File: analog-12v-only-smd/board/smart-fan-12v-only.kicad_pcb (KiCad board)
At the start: 2 copper layers, 62.2 x 41.3 mm, 31 parts, among them J1 KTY81/120, J2 12V_PWR, J3 12V_In, J4 FAN_Out, J5 FAN_Out, Q1 2N7000, Q2 FQP27P06, U1 LM358, U2 L7809, U3 NE555P

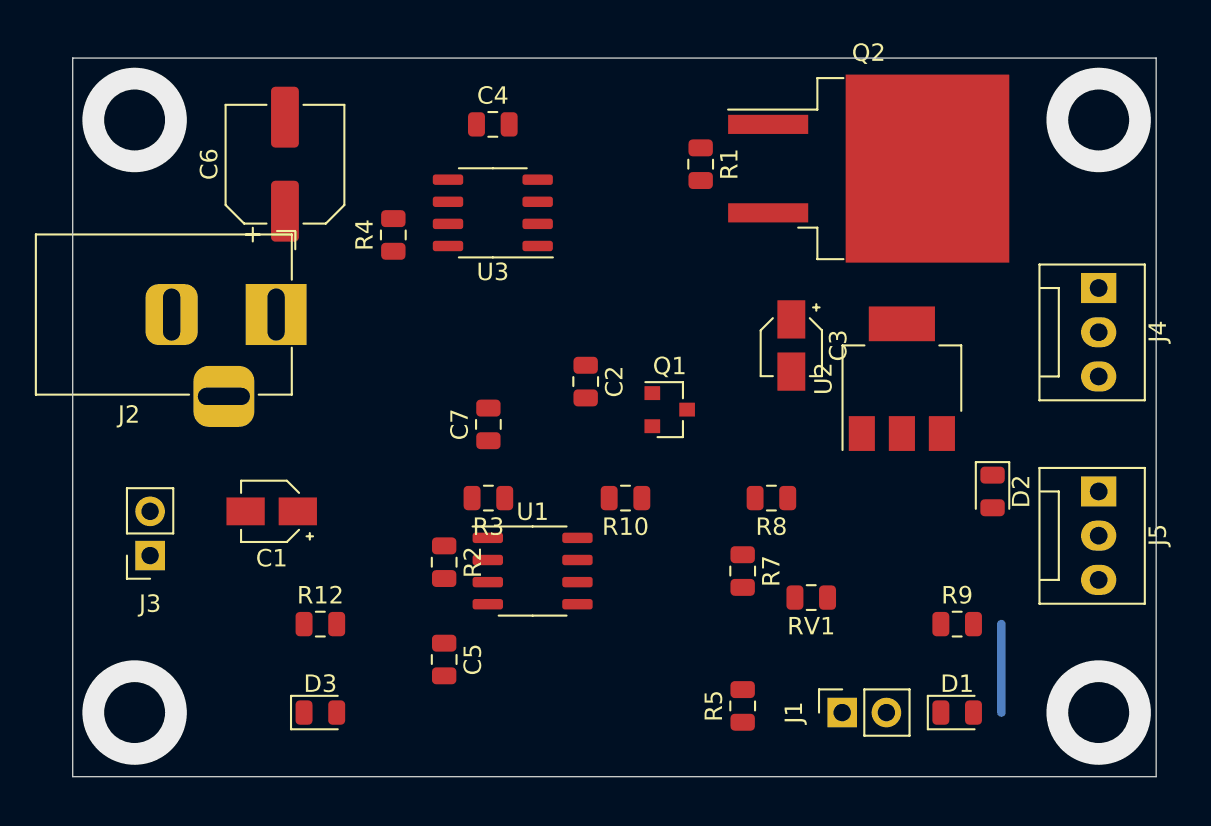
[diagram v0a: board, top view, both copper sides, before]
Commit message: Fix board layout
Power transistor drain-source swapped
Flyback diode reversed
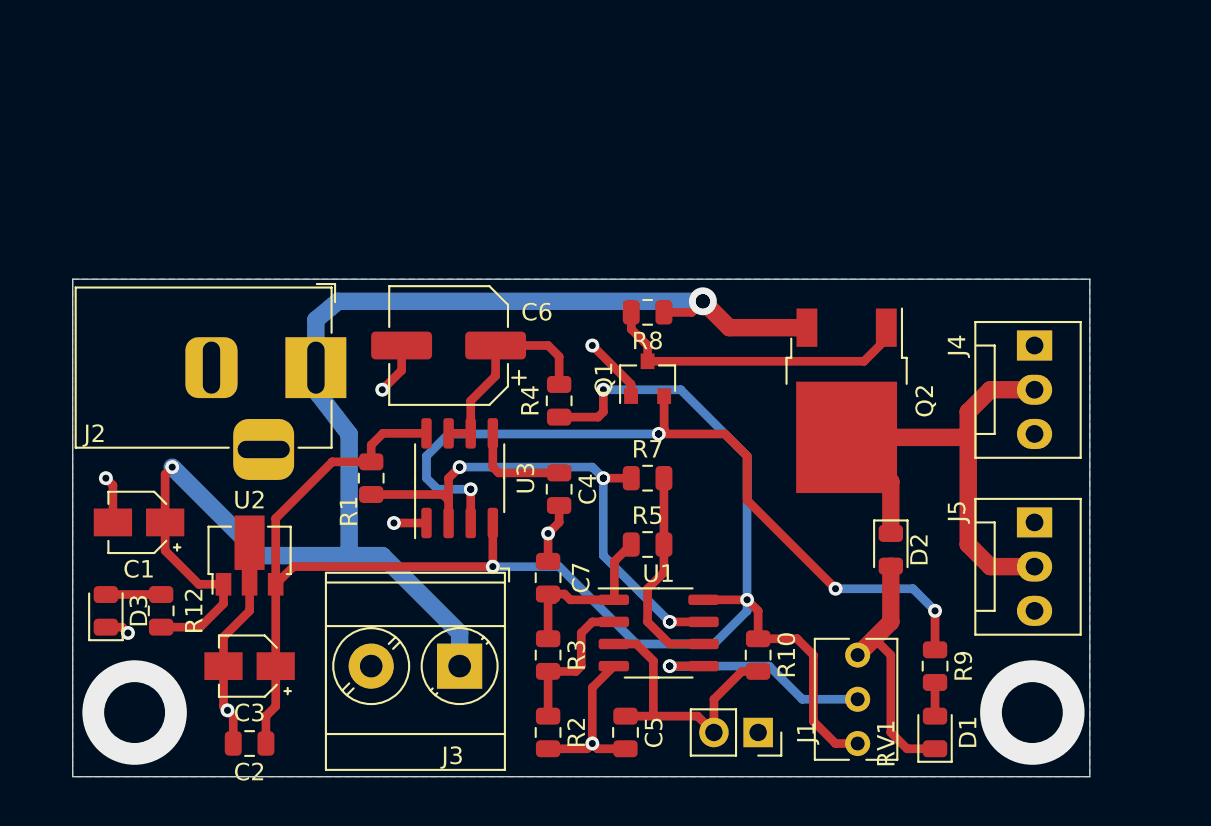
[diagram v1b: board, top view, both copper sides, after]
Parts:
- J3: footprint Connector_PinSocket_2.54mm:PinSocket_1x02_P2.54mm_Vertical -> TerminalBlock_Phoenix:TerminalBlock_Phoenix_MKDS-3-2-5.08_1x02_P5.08mm_Horizontal
- Q2: value FQP27P06 -> SUD19P06-60; footprint Package_TO_SOT_SMD:TO-263-2 -> Package_TO_SOT_SMD:TO-252-2
- R12: value 27k -> 5k
- R9: value 27k -> 3k3
- RV1: footprint Resistor_SMD:R_0805_2012Metric -> Potentiometer_THT:Potentiometer_Bourns_3266Y_Vertical
- U2: footprint Package_TO_SOT_SMD:SOT-223 -> Package_TO_SOT_SMD:SOT-89-3
- moved U2 38.8 mm to (114.8, 106.6)
- moved C3 36.2 mm to (114.8, 112.9), turned to 180 degrees
- moved C2 28.4 mm to (114.8, 117.3), turned to 180 degrees
- moved R1 26.1 mm to (121.8, 102.1)
- moved C4 21.3 mm to (132.6, 102.7), turned to 270 degrees
- moved J3 18.9 mm to (126.9, 112.9)
- moved U3 15.4 mm to (126.9, 102.1), turned to 90 degrees
- moved C6 14.0 mm to (126.2, 94.5), turned to 180 degrees
- moved D3 13.6 mm to (106.6, 109.7), turned to 90 degrees
- moved R4 13.5 mm to (132.6, 97.7)
- moved Q2 13.4 mm to (149.1, 97.7), turned to 270 degrees
- moved R8 12.8 mm to (137.7, 92.6)
- moved R10 11.8 mm to (144.0, 112.3), turned to 270 degrees
- moved R2 11.5 mm to (132.0, 116.7)
- moved C5 11.2 mm to (136.4, 116.7)
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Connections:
- D2 pad 1: GND -> Net-(D2-Pad1)
- D2 pad 2: Net-(D2-Pad2) -> GND
- J4 pad 2: Net-(D2-Pad2) -> Net-(D2-Pad1)
- J5 pad 2: Net-(D2-Pad2) -> Net-(D2-Pad1)
- Q2 pad 2: +12V -> Net-(D2-Pad1)
- Q2 pad 3: Net-(D2-Pad2) -> +12V
- R9 pad 1: Net-(D2-Pad2) -> Net-(Q1-Pad2)
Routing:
- net +9V: track 0.00 -> 95.1 mm, vias 0 -> 3
- net +12V: track 0.00 -> 82.6 mm, vias 0 -> 3
- net GND: track 0.00 -> 50.6 mm, vias 0 -> 8
- net Net-(Q1-Pad2): track 0.00 -> 46.0 mm, vias 0 -> 7
- net Trigger: track 0.00 -> 29.9 mm, vias 0 -> 8
- net Net-(D2-Pad1): track 0.00 -> 29.9 mm
- net Net-(Q1-Pad3): track 0.00 -> 18.1 mm
- net /TMP_IN: track 0.00 -> 16.4 mm
- net Net-(RV1-Pad2): track 0.00 -> 13.5 mm, vias 0 -> 3
- net Net-(C6-Pad1): track 0.00 -> 12.4 mm
- net Net-(R5-Pad2): track 0.00 -> 12.4 mm
- net Net-(C7-Pad1): track 0.00 -> 10.5 mm
- net Net-(R2-Pad1): track 0.00 -> 8.64 mm
- net Net-(C4-Pad1): track 0.00 -> 5.89 mm
- net Net-(D3-Pad2): track 0.00 -> 3.17 mm
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- added copper zone on B.Cu, net GND
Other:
- board size 62.2 x 41.3 mm -> 58.4 x 28.6 mm

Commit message: WIP: Cleaning up board
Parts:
- D2: value 1N5818 -> 1N5819HW; footprint Diode_SMD:D_0805_2012Metric -> Diode_SMD:D_SOD-123
- Q2: value SUD19P06-60 -> DMP4051LK3-13
- R10: value 10k -> 100k
